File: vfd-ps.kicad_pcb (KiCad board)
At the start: 2 copper layers, 0 parts

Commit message: Place all components on pcb
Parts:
- added C1: 22u, esynr3z_Capacitor:C_1210, F.Cu at (124.0, 60.5)
- added C10: 1.8n, esynr3z_Capacitor:C_0805, F.Cu at (146.1, 61.2)
- added C11: 22u, esynr3z_Capacitor:CP_Elec_6.3x7.7, F.Cu at (128.8, 36.3)
- added C12: 22u, esynr3z_Capacitor:C_1210, F.Cu at (144.0, 30.5)
- added C13: 22u, esynr3z_Capacitor:CP_Elec_6.3x7.7, F.Cu at (128.8, 24.6)
- added C14: 10n, esynr3z_Capacitor:C_0805, F.Cu at (154.3, 30.2)
- added C15: 1u, esynr3z_Capacitor:C_1206, F.Cu at (149.5, 34.2)
- added C2: 22u, esynr3z_Capacitor:C_1210, F.Cu at (127.3, 60.5)
- added C3: 22u, esynr3z_Capacitor:C_1210, F.Cu at (130.6, 60.5)
- added C4: 1u, esynr3z_Capacitor:C_1206, F.Cu at (130.6, 55.1)
- added C5: 100n, esynr3z_Capacitor:C_0805, F.Cu at (135.9, 57.4)
- added C6: 4.7u, esynr3z_Capacitor:C_1210, F.Cu at (130.6, 49.8)
- added C7: 4.7u, esynr3z_Capacitor:C_1210, F.Cu at (127.3, 49.8)
- added C8: 4.7u, esynr3z_Capacitor:C_1210, F.Cu at (124.0, 49.8)
- added C9: 220n, esynr3z_Capacitor:C_0805, F.Cu at (146.1, 57.4)
- added D1: MBRA340, esynr3z_Diode:SMA, F.Cu at (141.0, 54.6)
- added D2: BZX84C4V7, esynr3z_SOT:SOT-23, F.Cu at (126.7, 30.5)
- added J1: Conn_01x02, esynr3z_Connector:PinHeader_1x02_P2.54mm_Vertical, F.Cu at (120.1, 61.5)
- added J2: Conn_01x02, esynr3z_Connector:PinHeader_1x02_P2.54mm_Vertical, F.Cu at (120.1, 48.8)
- added J3: Conn_01x02, esynr3z_Connector:PinHeader_1x02_P2.54mm_Vertical, F.Cu at (120.3, 30.1)
- added JP1: SolderJumper_2_Bridged, esynr3z_Jumper:SolderJumper-2_P1.3mm_Bridged2Bar_RoundedPad1.0x1.5mm, F.Cu at (130.6, 30.5)
- added L1: 33u, esynr3z_Inductor:Sumida_CDRH127, F.Cu at (141.0, 45.7)
- added R1: dnf, esynr3z_Resistor:R_0805, F.Cu at (135.9, 61.2)
- added R10: 2.2k, esynr3z_Resistor:R_0805, F.Cu at (154.3, 26.4)
- added R11: 100, esynr3z_Resistor:R_0805, F.Cu at (123.7, 27.9)
- added R12: 10k, esynr3z_Resistor:R_0805, F.Cu at (149.5, 26.4)
- added R2: 16k, esynr3z_Resistor:R_0805, F.Cu at (146.1, 65.0)
- added R3: dnf, esynr3z_Resistor:R_0805, F.Cu at (133.6, 65.0)
- added R4: 220k, esynr3z_Resistor:R_0805, F.Cu at (135.9, 65.0)
- added R5: 6.8k, esynr3z_Resistor:R_0805, F.Cu at (148.3, 61.2)
- added R6: 1k, esynr3z_Resistor:R_0805, F.Cu at (148.3, 65.0)
- added R7: 100, esynr3z_Resistor:R_0805, F.Cu at (123.7, 33.0)
- added R8: 10k, esynr3z_Resistor:R_0805, F.Cu at (147.1, 26.4)
- added R9: 10k, esynr3z_Resistor:R_0805, F.Cu at (151.9, 26.4)
- added RV1: 20k, esynr3z_Potentiometer:Bourns_3362P, F.Cu at (141.0, 67.1)
- added RV2: 50, esynr3z_Potentiometer:Bourns_3362P, F.Cu at (138.4, 34.5)
- added RV3: 50, esynr3z_Potentiometer:Bourns_3362P, F.Cu at (138.4, 26.4)
- added TP1: TestPoint, esynr3z_TestPoint:TestPoint_THTPad_D1.5mm_Drill0.7mm, F.Cu at (148.3, 54.6)
- added TP2: TestPoint, esynr3z_TestPoint:TestPoint_THTPad_D1.5mm_Drill0.7mm, F.Cu at (144.0, 36.6)
- added TP3: TestPoint, esynr3z_TestPoint:TestPoint_THTPad_D1.5mm_Drill0.7mm, F.Cu at (144.0, 24.4)
- added U1: TPS54360DDA, esynr3z_SO:TI_SO-PowerPAD-8_ThermalVias, F.Cu at (141.0, 59.9)
- added U2: LM4871, esynr3z_SO:VSSOP-8_3.0x3.0mm_P0.65mm, F.Cu at (149.5, 30.6)

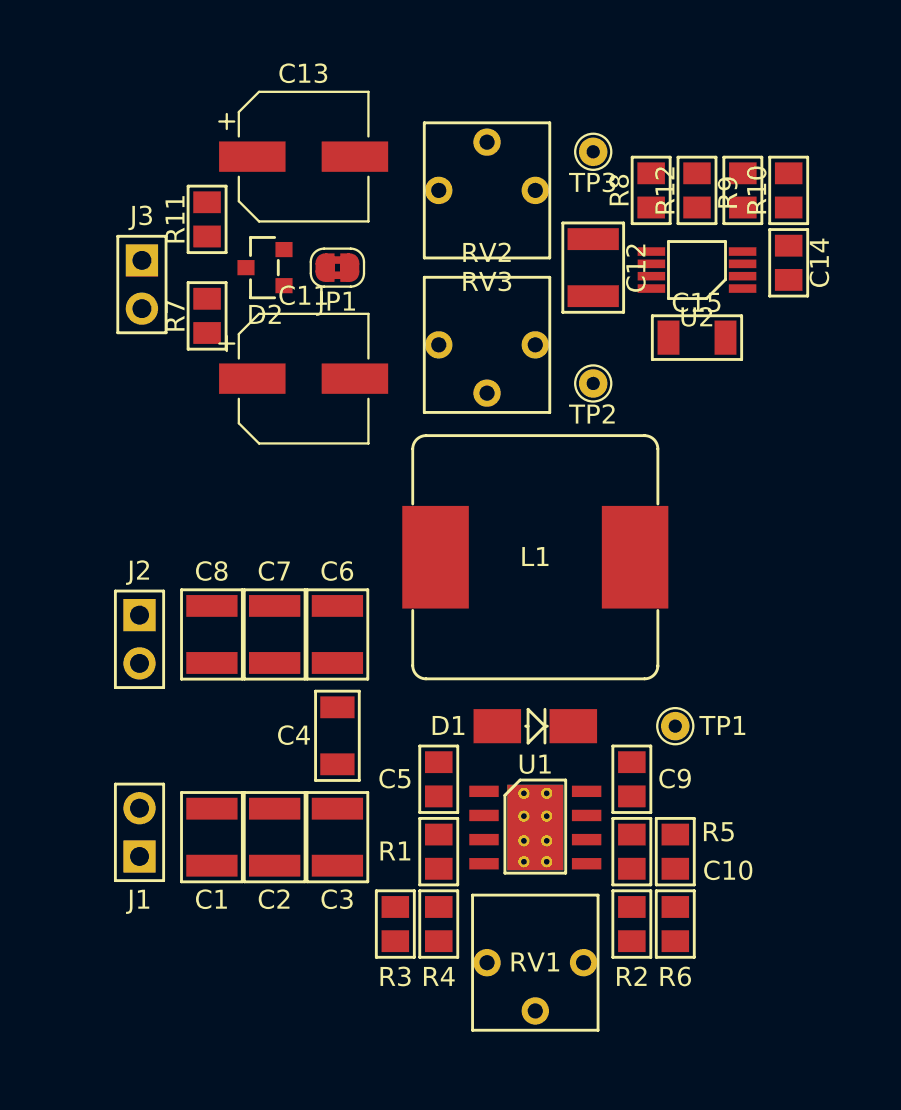
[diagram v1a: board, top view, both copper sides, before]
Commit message: Place all references on silk layer
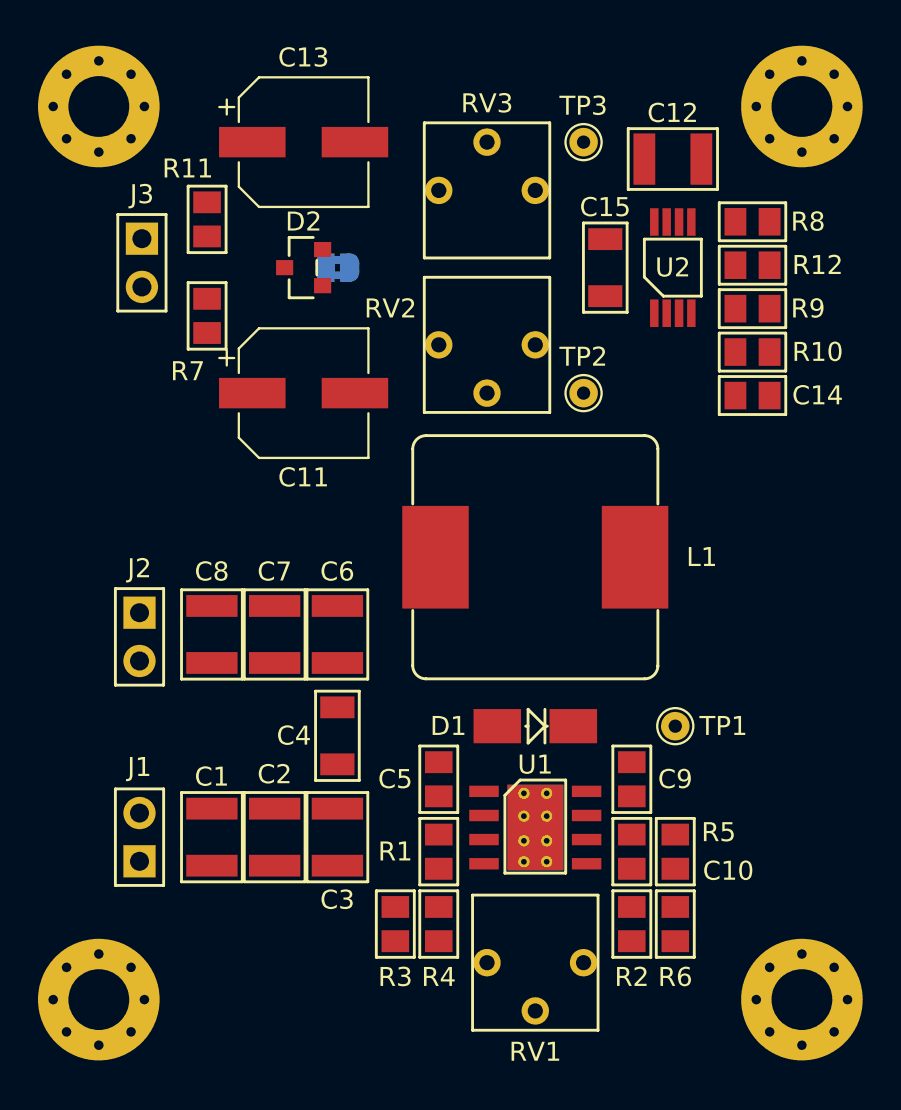
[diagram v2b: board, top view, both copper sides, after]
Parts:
- added REF**: MountingHole_3.2mm_M3_Pad_Via, MountingHole:MountingHole_3.2mm_M3_Pad_Via, F.Cu at (155.0, 69.0)
- added REF**: MountingHole_3.2mm_M3_Pad_Via, MountingHole:MountingHole_3.2mm_M3_Pad_Via, F.Cu at (118.0, 69.0)
- added REF**: MountingHole_3.2mm_M3_Pad_Via, MountingHole:MountingHole_3.2mm_M3_Pad_Via, F.Cu at (155.0, 22.0)
- added REF**: MountingHole_3.2mm_M3_Pad_Via, MountingHole:MountingHole_3.2mm_M3_Pad_Via, F.Cu at (118.0, 22.0)
- JP1: moved to B.Cu
- moved R10 8.72 mm to (152.4, 34.9), turned to 0 degrees
- moved C14 7.24 mm to (152.4, 37.2), turned to 0 degrees
- moved C12 7.09 mm to (148.2, 24.8), turned to 180 degrees
- moved R9 6.24 mm to (152.4, 32.6), turned to 0 degrees
- moved C15 6.07 mm to (144.7, 30.5), turned to 270 degrees
- moved R8 5.58 mm to (152.4, 28.1), turned to 0 degrees
- moved R12 4.90 mm to (152.4, 30.4), turned to 0 degrees
- moved D2 2.03 mm to (128.8, 30.5)
- moved U2 1.28 mm to (148.2, 30.5), turned to 90 degrees
- moved J3 1.14 mm to (120.3, 29.0)
- moved C11 0.76 mm to (128.8, 37.1)
- moved C13 0.76 mm to (128.8, 23.9)
- moved TP2 0.72 mm to (143.5, 37.1)
- moved TP3 0.72 mm to (143.5, 23.9)
- moved J1 0.25 mm to (120.1, 61.7)
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
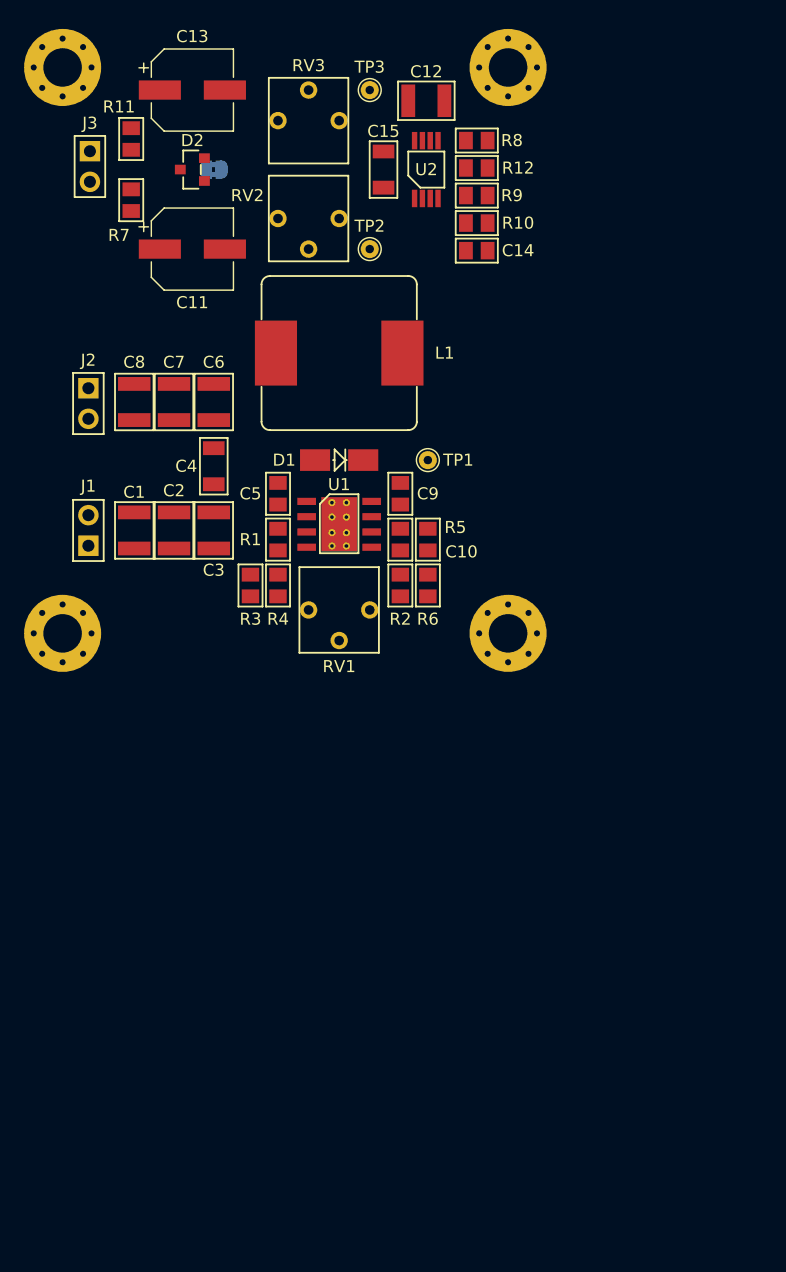
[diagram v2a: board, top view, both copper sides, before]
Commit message: Minor components placement tweaks
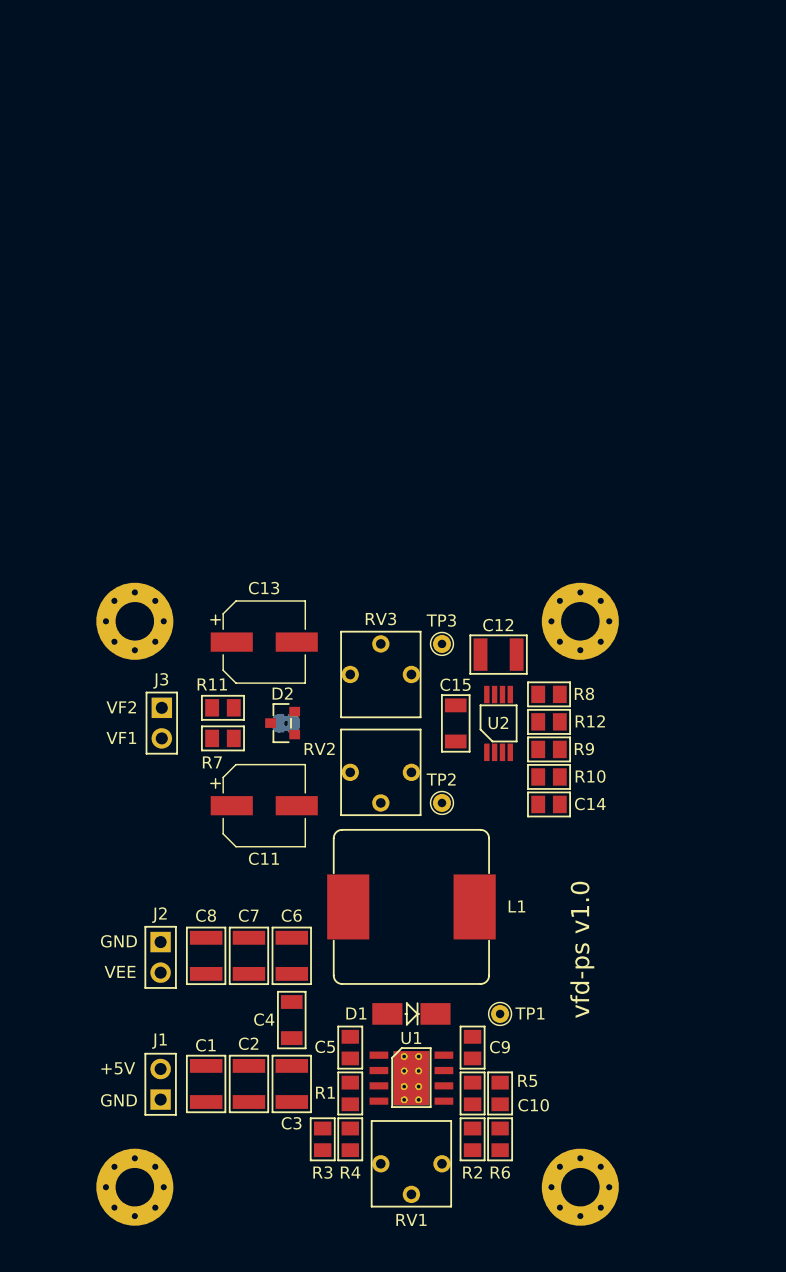
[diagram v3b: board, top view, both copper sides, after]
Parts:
- moved R11 47.9 mm to (131.3, 75.2), turned to 180 degrees
- moved C11 46.6 mm to (134.7, 83.3)
- moved J3 46.6 mm to (126.2, 75.2)
- moved D2 46.6 mm to (136.3, 76.5)
- moved C6 46.5 mm to (137.0, 95.8)
- moved C4 46.5 mm to (137.0, 101.1)
- moved C3 46.4 mm to (137.0, 106.4)
- moved C7 46.4 mm to (133.5, 95.8)
- moved C2 46.4 mm to (133.5, 106.4)
- moved J2 46.4 mm to (126.1, 94.6)
- moved C10 46.4 mm to (152.1, 107.2)
- moved C12 46.4 mm to (154.2, 70.8)
- moved C14 46.4 mm to (158.4, 83.2)
- moved C15 46.4 mm to (150.7, 76.5)
- moved D1 46.4 mm to (147.0, 100.6)
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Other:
- board text added: "+5V"
- board text added: "GND"
- board text added: "VEE"
- board text added: "VF1"
- board text added: "VF2"
- board text added: "vfd-ps v1.0"

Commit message: Replace connectors, add testpoints, pcb rotate and align
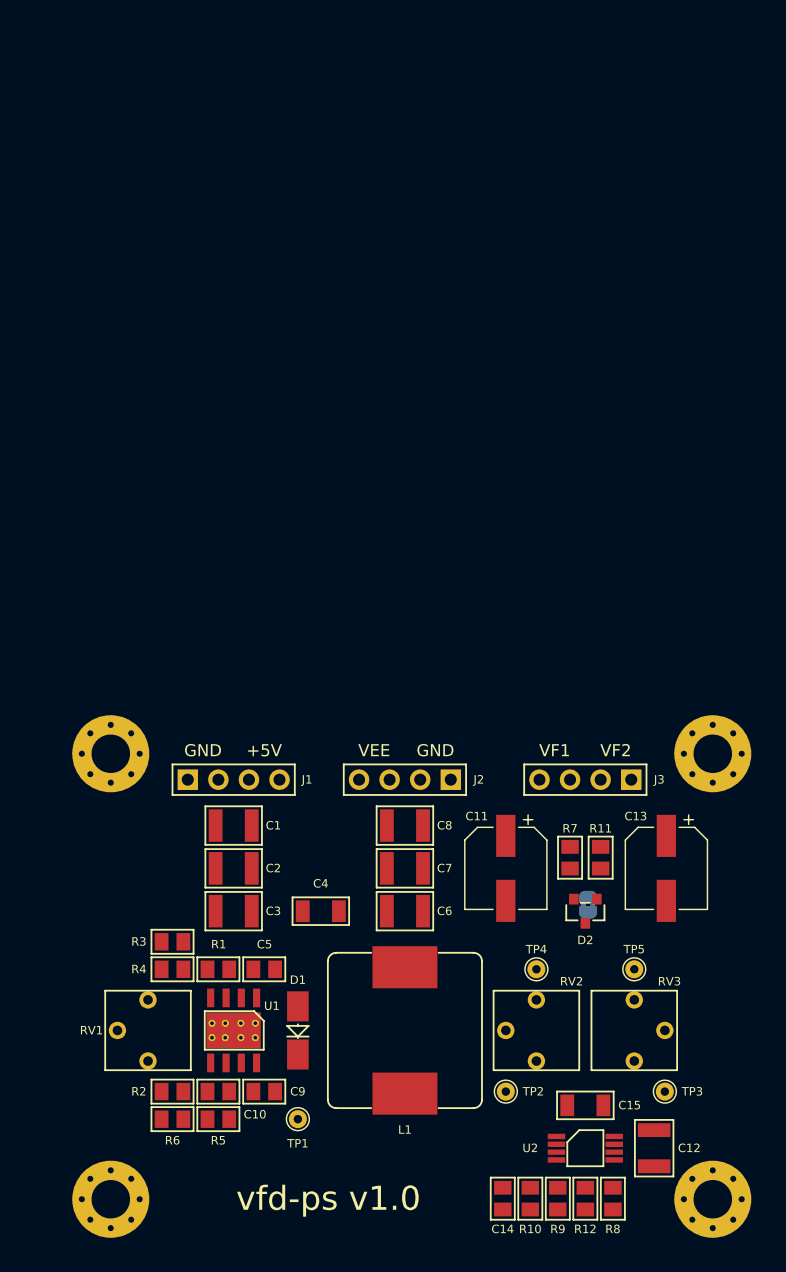
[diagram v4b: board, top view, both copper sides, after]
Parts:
- added TP4: TestPoint, esynr3z_TestPoint:TestPoint_THTPad_D1.5mm_Drill0.7mm, F.Cu at (157.4, 96.9)
- added TP5: TestPoint, esynr3z_TestPoint:TestPoint_THTPad_D1.5mm_Drill0.7mm, F.Cu at (165.5, 96.9)
- J1, J2, J3: value Conn_01x02 -> Conn_01x04; footprint esynr3z_Connector:PinHeader_1x02_P2.54mm_Vertical -> esynr3z_Connector:PinHeader_1x04_P2.54mm_Vertical
- moved REF** 49.2 mm to (172.0, 116.0), turned to 270 degrees
- moved REF** 49.2 mm to (172.0, 79.0), turned to 270 degrees
- moved C12 43.0 mm to (167.1, 111.8), turned to 90 degrees
- moved R8 42.2 mm to (163.7, 116.0), turned to 270 degrees
- moved TP3 41.5 mm to (168.0, 107.1), turned to 90 degrees
- moved R12 39.7 mm to (161.4, 116.0), turned to 270 degrees
- moved J3 39.4 mm to (165.2, 81.2), turned to 270 degrees
- moved REF** 39.0 mm to (122.0, 116.0), turned to 270 degrees
- moved C13 38.3 mm to (168.1, 88.5), turned to 270 degrees
- moved R9 37.3 mm to (159.1, 116.0), turned to 270 degrees
- moved RV3 36.3 mm to (165.5, 102.0), turned to 90 degrees
- moved REF** 36.1 mm to (122.0, 79.0), turned to 270 degrees
- moved U2 36.0 mm to (161.4, 111.8), turned to 0 degrees
- moved R10 35.1 mm to (156.8, 116.0), turned to 270 degrees
- moved R11 33.7 mm to (162.7, 87.6), turned to 90 degrees
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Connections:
- J1 pad 2: +5V -> GND
- J2 pad 2: GNDPAD -> GND
- J3 pad 2: VF1 -> VF2

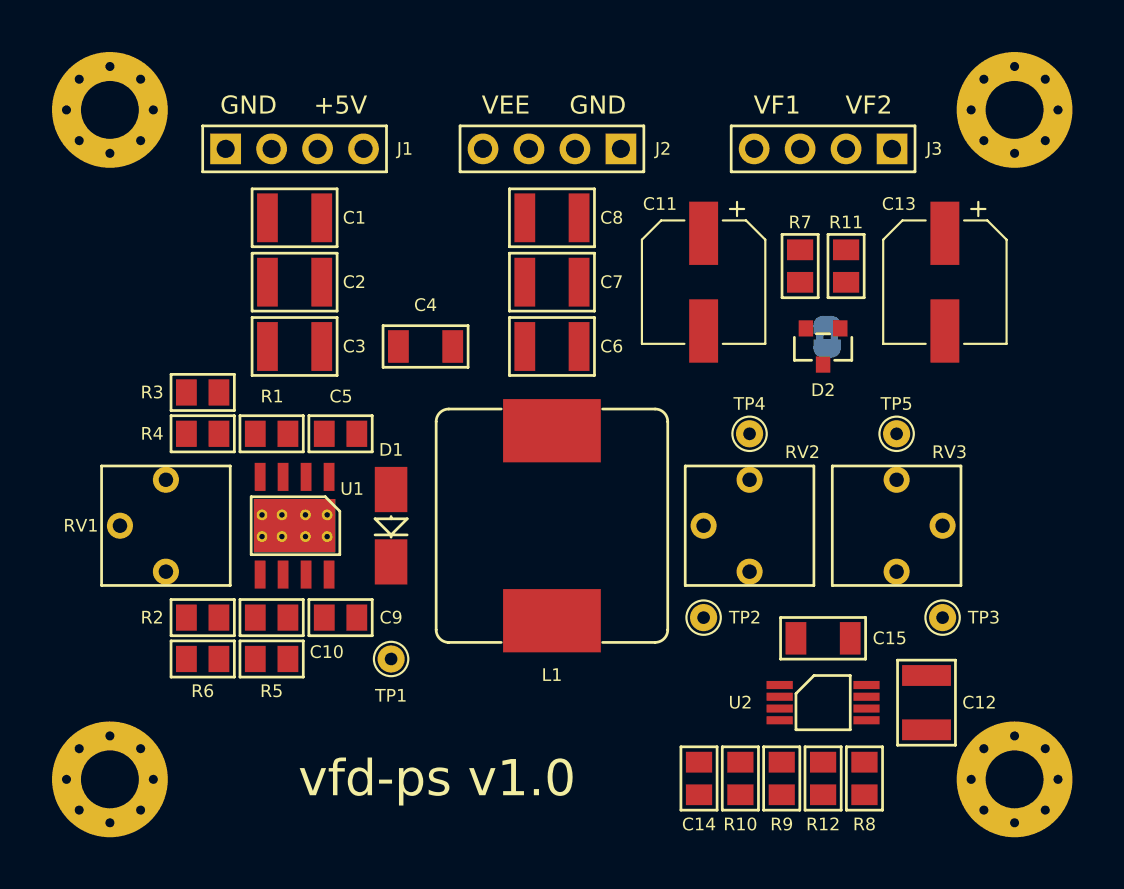
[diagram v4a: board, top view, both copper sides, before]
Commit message: Trace buck-boost pcb part
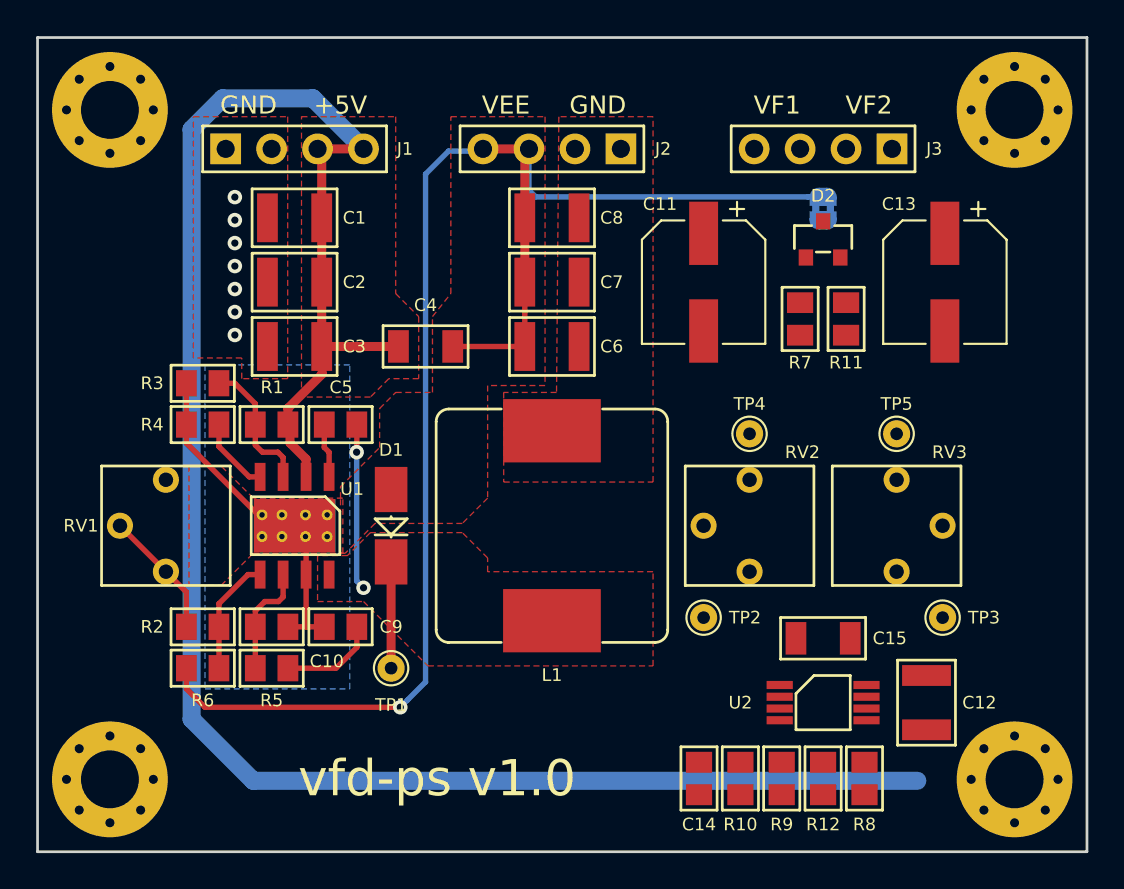
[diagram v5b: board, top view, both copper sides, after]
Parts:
- moved JP1 7.08 mm to (161.4, 84.5), turned to 270 degrees
- moved D2 5.92 mm to (161.4, 86.2), turned to 90 degrees
- moved R11 2.92 mm to (162.7, 90.6), turned to 270 degrees
- moved R7 2.92 mm to (160.1, 90.6), turned to 90 degrees
- moved R5 0.51 mm to (130.9, 109.9)
- moved R6 0.51 mm to (127.1, 109.9)
- moved TP1 0.51 mm to (137.5, 109.9)
- moved C10 0.51 mm to (130.9, 107.6)
- moved C5 0.51 mm to (134.7, 96.4)
- moved C9 0.51 mm to (134.7, 107.6)
- moved R1 0.51 mm to (130.9, 96.4)
- moved R2 0.51 mm to (127.1, 107.6)
- moved R3 0.51 mm to (127.1, 94.1)
- moved R4 0.51 mm to (127.1, 96.4)
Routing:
- net +5V: track 0.00 -> 111.7 mm
- net GNDPAD: track 0.00 -> 99.5 mm, vias 0 -> 1
- net Net-(C5-Pad2): track 0.00 -> 15.1 mm, vias 0 -> 2
- net Net-(R1-Pad2): track 0.00 -> 7.66 mm
- net Net-(R2-Pad1): track 0.00 -> 7.11 mm
- net Net-(R2-Pad2): track 0.00 -> 6.51 mm
- net Net-(C10-Pad1): track 0.00 -> 6.26 mm
- net Net-(C9-Pad1): track 0.00 -> 5.42 mm
- net Net-(R4-Pad1): track 0.00 -> 4.18 mm
- net Net-(C5-Pad1): track 0.00 -> 3.00 mm
- net GND: vias 0 -> 7
- added copper zone on F.Cu, net +5V
- added copper zone on B.Cu, net GND
- added copper zone on F.Cu, net GND
- added copper zone on B.Cu, net GNDPAD
- added copper zone on F.Cu, net GNDPAD
- added copper zone on F.Cu, net Net-(C5-Pad2)
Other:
- board outline added: 58 x 45 mm
- net class Default: trace_width 0.25 -> 0.3
